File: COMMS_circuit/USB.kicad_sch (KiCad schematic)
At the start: 24 parts, among them J3 USB_C_Receptacle_USB2.0_14P, U10 FT2232HL, U11 93LC56, X3 SIT9003AI-13-33DB-12.00000Y

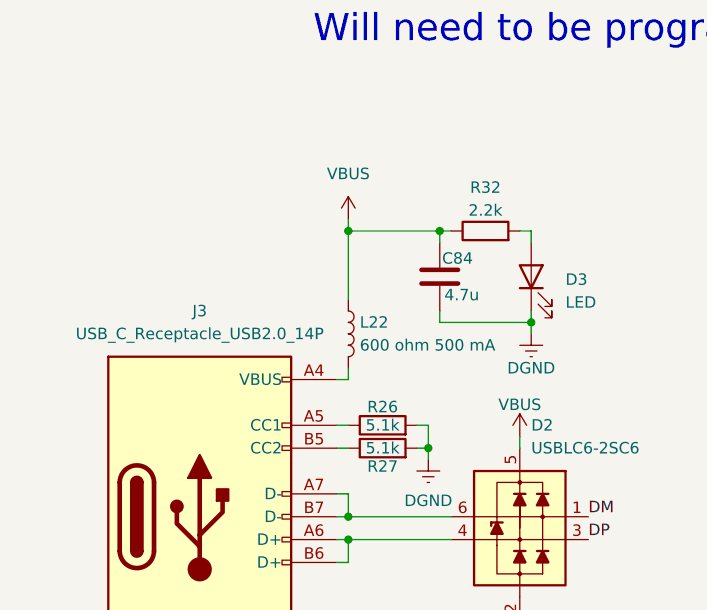
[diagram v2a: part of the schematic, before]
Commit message: switching the VBUS to RP2040 USB cause its more sensical
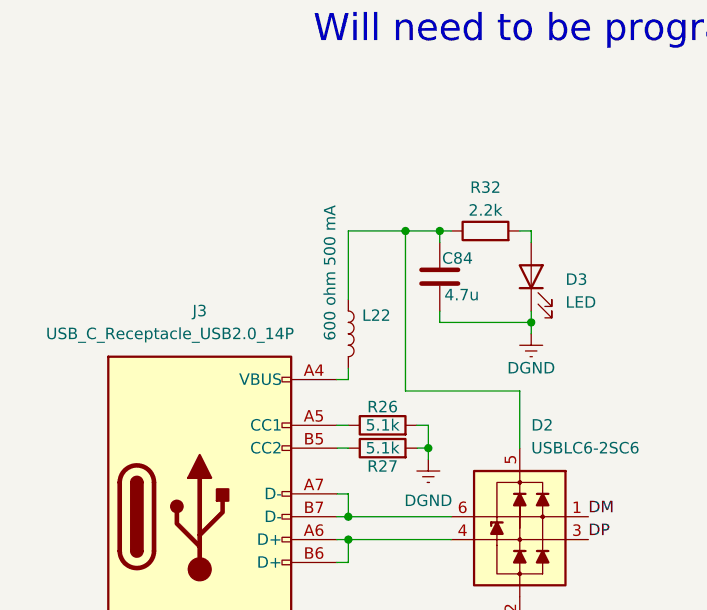
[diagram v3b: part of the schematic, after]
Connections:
- net VBUS: no longer names the net of C84.1, D2.5 (VP), L22.1, R32.1
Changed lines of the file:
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@@
 	)
 	(junction
-		(at 58.42 49.53)
-		(diameter 0)
-		(color 0 0 0 0)
-	)
-	(junction
 		(at 58.42 83.82)
 		(diameter 0)
@@
 	)
 	(junction
+		(at 64.77 49.53)
+		(diameter 0)
+		(color 0 0 0 0)
+	)
+	(junction
 		(at 58.42 81.28)
 		(diameter 0)
@@
 	(wire
 		(pts
-			(xy 58.42 49.53) (xy 68.58 49.53)
+			(xy 64.77 67.31) (xy 64.77 49.53)
+		)
+		(stroke
+			(width 0)
+			(type default)
+		)
+	)
+	(wire
+		(pts
+			(xy 58.42 49.53) (xy 64.77 49.53)
 		)
 		(stroke
@@
 	(wire
 		(pts
+			(xy 77.47 67.31) (xy 64.77 67.31)
+		)
+		(stroke
+			(width 0)
+			(type default)
+		)
+	)
+	(wire
+		(pts
 			(xy 185.42 152.4) (xy 185.42 153.67)
 		)
@@
 	(wire
 		(pts
-			(xy 77.47 72.39) (xy 77.47 73.66)
+			(xy 77.47 67.31) (xy 77.47 73.66)
 		)
 		(stroke
@@
 	(wire
 		(pts
+			(xy 64.77 49.53) (xy 68.58 49.53)
+		)
+		(stroke
+			(width 0)
+			(type default)
+		)
+	)
+	(wire
+		(pts
 			(xy 175.26 39.37) (xy 177.8 39.37)
 		)
@@
 	(wire
 		(pts
-			(xy 58.42 48.26) (xy 58.42 49.53)
-		)
-		(stroke
-			(width 0)
-			(type default)
-		)
-	)
-	(wire
-		(pts
 			(xy 135.89 127) (xy 149.86 127)
 		)
@@
 	)
 	(symbol
-		(lib_id "power:VBUS")
-		(at 77.47 72.39 0)
-		(unit 1)
-		(exclude_from_sim no)
-		(in_bom yes)
-		(on_board yes)
-		(dnp no)
-		(property "Reference" "#PWR088"
-			(at 77.47 76.2 0)
-			(effects
-				(font
-					(size 1.27 1.27)
-				)
-				(hide yes)
-			)
-		)
-		(property "Value" "VBUS"
-			(at 77.47 68.834 0)
-			(effects
-				(font
-					(size 1.27 1.27)
-				)
-			)
-		)
-		(property "Footprint" ""
-			(at 77.47 72.39 0)
-			(effects
-				(font
-					(size 1.27 1.27)
-				)
-				(hide yes)
-			)
-		)
-		(property "Datasheet" ""
-			(at 77.47 72.39 0)
-			(effects
-				(font
-					(size 1.27 1.27)
-				)
-				(hide yes)
-			)
-		)
-		(property "Description" "Power symbol creates a global label with name \"VBUS\""
-			(at 77.47 72.39 0)
-			(effects
-				(font
-					(size 1.27 1.27)
-				)
-				(hide yes)
-			)
-		)
-		(pin "1"
-		)
-		(instances
-			(project "COMMS_circuit"
-				(path "/bdd480c2-e959-4f78-bdcb-24d46c5e40e4/e39025b8-a3d3-497e-917d-d3b2eef3ce4b"
-					(reference "#PWR088")
-					(unit 1)
-				)
-			)
-		)
-	)
-	(symbol
 		(lib_id "Device:C")
 		(at 162.56 34.29 0)
@@
 		(on_board yes)
 		(dnp no)
-		(fields_autoplaced yes)
 		(property "Reference" "L22"
-			(at 59.69 59.6899 0)
+			(at 59.944 58.928 0)
 			(effects
 				(font
@@
 		)
 		(property "Value" "600 ohm 500 mA"
-			(at 59.69 62.2299 0)
+			(at 56.388 61.722 90)
 			(effects
 				(font
@@
 		(on_board yes)
 		(dnp no)
-		(fields_autoplaced yes)
 		(property "Reference" "J3"
 			(at 41.91 58.42 0)
@@
 		)
 		(property "Value" "USB_C_Receptacle_USB2.0_14P"
-			(at 41.91 60.96 0)
+			(at 38.608 60.96 0)
 			(effects
 				(font
@@
 					(unit 1)
 				)
-			)
-		)
-	)
-	(symbol
-		(lib_id "power:VBUS")
-		(at 58.42 48.26 0)
-		(unit 1)
-		(exclude_from_sim no)
-		(in_bom yes)
-		(on_board yes)
-		(dnp no)
-		(fields_autoplaced yes)
-		(property "Reference" "#PWR084"
-			(at 58.42 52.07 0)
-			(effects
-				(font
-					(size 1.27 1.27)
-				)
-				(hide yes)
-			)
-		)
-		(property "Value" "VBUS"
-			(at 58.42 43.18 0)
-			(effects
-				(font
-					(size 1.27 1.27)
-				)
-			)
-		)
-		(property "Footprint" ""
-			(at 58.42 48.26 0)
-			(effects
-				(font
-					(size 1.27 1.27)
-				)
-				(hide yes)
-			)
-		)
-		(property "Datasheet" ""
-			(at 58.42 48.26 0)
-			(effects
-				(font
-					(size 1.27 1.27)
-				)
-				(hide yes)
-			)
-		)
-		(property "Description" "Power symbol creates a global label with name \"VBUS\""
-			(at 58.42 48.26 0)
-			(effects
-				(font
-					(size 1.27 1.27)
-				)
-				(hide yes)
-			)
-		)
-		(pin "1"
-		)
-		(instances
-			(project "COMMS_circuit"
-				(path "/bdd480c2-e959-4f78-bdcb-24d46c5e40e4/e39025b8-a3d3-497e-917d-d3b2eef3ce4b"
-					(reference "#PWR084")
-					(unit 1)
-				)
